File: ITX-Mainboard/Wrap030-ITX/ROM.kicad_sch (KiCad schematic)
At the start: 3 parts

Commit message: Schematic substantial completion
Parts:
- C17: footprint Capacitor_SMD:C_0805_2012Metric -> Capacitor_SMD:C_0402_1005Metric_Pad0.74x0.62mm_HandSolder; JLC-Part (none) -> https://jlcpcb.com/partdetail/1877-CL05B104KO5NNNC/C1525
- C18: footprint Capacitor_SMD:C_0805_2012Metric -> Capacitor_SMD:C_0402_1005Metric_Pad0.74x0.62mm_HandSolder; JLC-Part (none) -> https://jlcpcb.com/partdetail/53938-CL05A105KA5NQNC/C52923
- ROM1: footprint (none) -> Package_LCC:PLCC-32_THT-Socket
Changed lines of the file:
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@@
       (effects (font (size 1.27 1.27)) (justify left))
     )
-    (property "Footprint" "" (at 81.28 66.04 0)
+    (property "Footprint" "Package_LCC:PLCC-32_THT-Socket" (at 81.28 66.04 0)
       (effects (font (size 1.27 1.27)) hide)
     )
     (property "Datasheet" "http://ww1.microchip.com/downloads/en/DeviceDoc/25022B.pdf" (at 81.28 66.04 0)
+      (effects (font (size 1.27 1.27)) hide)
+    )
+    (property "JLC-Part" "" (at 81.28 73.66 0)
+      (effects (font (size 1.27 1.27)) hide)
+    )
+    (property "Mouser-Part" "" (at 81.28 73.66 0)
+      (effects (font (size 1.27 1.27)) hide)
+    )
+    (property "Notes" "" (at 81.28 73.66 0)
       (effects (font (size 1.27 1.27)) hide)
     )
@@
       (effects (font (size 1.27 1.27)) (justify left))
     )
-    (property "Footprint" "Capacitor_SMD:C_0805_2012Metric" (at 101.6 73.66 0)
+    (property "Footprint" "Capacitor_SMD:C_0402_1005Metric_Pad0.74x0.62mm_HandSolder" (at 101.6 73.66 0)
       (effects (font (size 1.27 1.27)) hide)
     )
     (property "Datasheet" "~" (at 101.6 73.66 0)
+      (effects (font (size 1.27 1.27)) hide)
+    )
+    (property "JLC-Part" "https://jlcpcb.com/partdetail/53938-CL05A105KA5NQNC/C52923" (at 101.6 73.66 0)
+      (effects (font (size 1.27 1.27)) hide)
+    )
+    (property "Mouser-Part" "" (at 101.6 73.66 0)
+      (effects (font (size 1.27 1.27)) hide)
+    )
+    (property "Notes" "" (at 101.6 73.66 0)
       (effects (font (size 1.27 1.27)) hide)
     )
@@
       (effects (font (size 1.27 1.27)) (justify left))
     )
-    (property "Footprint" "Capacitor_SMD:C_0805_2012Metric" (at 96.52 73.66 0)
+    (property "Footprint" "Capacitor_SMD:C_0402_1005Metric_Pad0.74x0.62mm_HandSolder" (at 96.52 73.66 0)
       (effects (font (size 1.27 1.27)) hide)
     )
@@
       (effects (font (size 1.27 1.27)) hide)
     )
+    (property "JLC-Part" "https://jlcpcb.com/partdetail/1877-CL05B104KO5NNNC/C1525" (at 96.52 73.66 0)
+      (effects (font (size 1.27 1.27)) hide)
+    )
+    (property "Mouser-Part" "" (at 96.52 73.66 0)
+      (effects (font (size 1.27 1.27)) hide)
+    )
+    (property "Notes" "" (at 96.52 73.66 0)
+      (effects (font (size 1.27 1.27)) hide)
+    )

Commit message: Completing PCB Routing
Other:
- title: Wrap030 ITX -> Wrap030-ATX Mainboard
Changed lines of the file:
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@@
   (paper "USLetter")
   (title_block
-    (title "Wrap030 ITX")
-    (date "2023-03-15")
-    (rev "0")
+    (title "Wrap030-ATX Mainboard")
+    (date "2023-03-26")
+    (rev "1")
     (company "techav")
   )

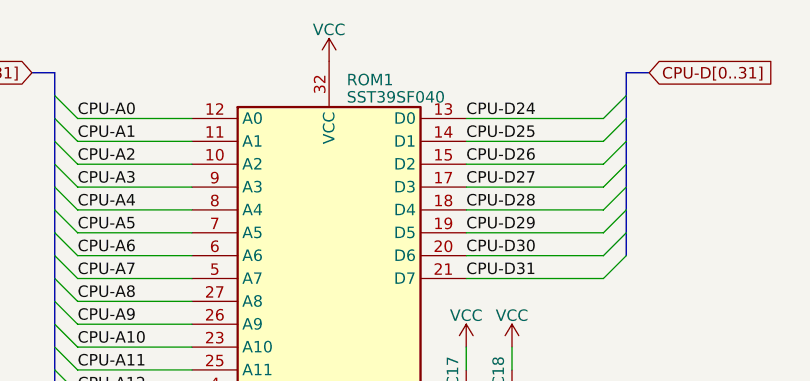
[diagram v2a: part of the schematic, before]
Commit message: PCB Silkscreen & DRC Cleanup
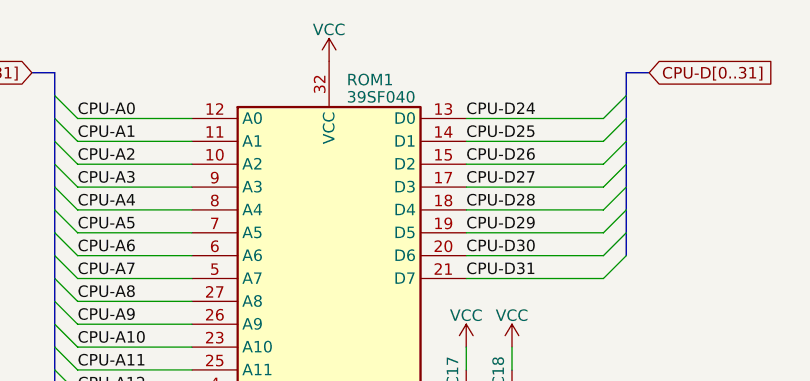
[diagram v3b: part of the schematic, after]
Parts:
- ROM1: value SST39SF040 -> 39SF040
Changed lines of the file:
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@@
       (effects (font (size 1.27 1.27)) (justify left))
     )
-    (property "Value" "SST39SF040" (at 83.2359 40.8211 0)
+    (property "Value" "39SF040" (at 83.2359 40.8211 0)
       (effects (font (size 1.27 1.27)) (justify left))
     )

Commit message: Replace resistor nets with 0402 & update gerbers
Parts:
- C17: Mouser-Part (none) -> 187-CL05B104KO5NNNC; Notes (none) -> JLC
- C18: Mouser-Part (none) -> 187-CL05A105KA5NQNC; Notes (none) -> JLC
- ROM1: Mouser-Part (none) -> 804-39SF0407CNHE; Notes (none) -> OFE; Socket-Mouser (none) -> 575-943224
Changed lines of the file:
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@@
       (effects (font (size 1.27 1.27)) hide)
     )
-    (property "Mouser-Part" "" (at 81.28 73.66 0)
+    (property "Mouser-Part" "804-39SF0407CNHE" (at 81.28 73.66 0)
       (effects (font (size 1.27 1.27)) hide)
     )
-    (property "Notes" "" (at 81.28 73.66 0)
+    (property "Notes" "OFE" (at 81.28 73.66 0)
+      (effects (font (size 1.27 1.27)) hide)
+    )
+    (property "Socket-Mouser" "575-943224" (at 81.28 73.66 0)
       (effects (font (size 1.27 1.27)) hide)
     )
@@
       (effects (font (size 1.27 1.27)) hide)
     )
-    (property "Mouser-Part" "" (at 101.6 73.66 0)
+    (property "Mouser-Part" "187-CL05A105KA5NQNC" (at 101.6 73.66 0)
       (effects (font (size 1.27 1.27)) hide)
     )
-    (property "Notes" "" (at 101.6 73.66 0)
+    (property "Notes" "JLC" (at 101.6 73.66 0)
+      (effects (font (size 1.27 1.27)) hide)
+    )
+    (property "Socket-Mouser" "" (at 101.6 73.66 0)
       (effects (font (size 1.27 1.27)) hide)
     )
@@
       (effects (font (size 1.27 1.27)) hide)
     )
-    (property "Mouser-Part" "" (at 96.52 73.66 0)
+    (property "Mouser-Part" "187-CL05B104KO5NNNC" (at 96.52 73.66 0)
       (effects (font (size 1.27 1.27)) hide)
     )
-    (property "Notes" "" (at 96.52 73.66 0)
+    (property "Notes" "JLC" (at 96.52 73.66 0)
       (effects (font (size 1.27 1.27)) hide)
     )
+    (property "Socket-Mouser" "" (at 96.52 73.66 0)
+      (effects (font (size 1.27 1.27)) hide)
+    )
